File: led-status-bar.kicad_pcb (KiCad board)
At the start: 2 copper layers, 2 parts

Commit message: Revision 1 commit
- Added all required connections to the PCB
- Fabrication revision 1
- Added README with suitable information
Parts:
- added C1: 100nF, Capacitor_SMD:C_0603_1608Metric_Pad1.08x0.95mm_HandSolder, F.Cu at (126.1, 79.8)
- added C2: 100nF, Capacitor_SMD:C_0603_1608Metric_Pad1.08x0.95mm_HandSolder, F.Cu at (126.1, 85.9)
- added C3: 100nF, Capacitor_SMD:C_0603_1608Metric_Pad1.08x0.95mm_HandSolder, F.Cu at (126.1, 92.1)
- added C4: 100nF, Capacitor_SMD:C_0603_1608Metric_Pad1.08x0.95mm_HandSolder, F.Cu at (126.1, 98.2)
- added C5: 100nF, Capacitor_SMD:C_0603_1608Metric_Pad1.08x0.95mm_HandSolder, F.Cu at (126.1, 104.3)
- added D1: WS2812B, LED_SMD:LED_WS2812B_PLCC4_5.0x5.0mm_P3.2mm, F.Cu at (131.1, 79.8)
- added D2: WS2812B, LED_SMD:LED_WS2812B_PLCC4_5.0x5.0mm_P3.2mm, F.Cu at (131.1, 85.9)
- added D3: WS2812B, LED_SMD:LED_WS2812B_PLCC4_5.0x5.0mm_P3.2mm, F.Cu at (131.1, 92.0)
- added D4: WS2812B, LED_SMD:LED_WS2812B_PLCC4_5.0x5.0mm_P3.2mm, F.Cu at (131.1, 98.1)
- added D5: WS2812B, LED_SMD:LED_WS2812B_PLCC4_5.0x5.0mm_P3.2mm, F.Cu at (131.1, 104.2)
- added H1: MountingHole, MountingHole:MountingHole_3.2mm_M3-smallBorder, F.Cu at (131.3, 61.2)
- added H2: MountingHole, MountingHole:MountingHole_3.2mm_M3-smallBorder, F.Cu at (131.3, 111.5)
- added J1: Conn_01x03, Connector_PinHeader_2.54mm:PinHeader_1x03_P2.54mm_Vertical, F.Cu at (128.8, 67.1)
- added Q1: SS8050-G, Package_TO_SOT_SMD:SOT-23, F.Cu at (129.0, 71.9)
- added R1: 1k, Resistor_SMD:R_0603_1608Metric_Pad0.98x0.95mm_HandSolder, F.Cu at (131.8, 71.9)
- moved G*** 150.1 mm to (129.8, 72.4), turned to -90 degrees
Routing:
- net VSS: track 0.00 -> 55.0 mm
- net GND: track 0.00 -> 14.0 mm, vias 0 -> 10
- net Net-(D1-Pad4): track 0.00 -> 7.27 mm
- net Net-(D4-Pad2): track 0.00 -> 6.10 mm
- net Net-(D3-Pad2): track 0.00 -> 6.10 mm
- net Net-(D2-Pad2): track 0.00 -> 6.10 mm
- net Net-(D1-Pad2): track 0.00 -> 6.10 mm
- net LED_CTRL: track 0.00 -> 4.22 mm
- net Net-(Q1-Pad1): track 0.00 -> 3.12 mm
- added copper zone on B.Cu, net GND
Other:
- board outline added: 15 x 57.4 mm
- board text added: "RGB-Led Status Bar v1.0 (2023)"

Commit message: Added pinout to back of board
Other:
- board text added: "DTA"
- board text added: "GND"
- board text added: "VSS"
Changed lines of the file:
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@@
   )
   (gr_rect (start 122.682 57.912) (end 137.668 115.316) (layer "Edge.Cuts") (width 0.2) (fill none))
+  (gr_text "DTA" (at 131.318 64.516) (layer "B.SilkS")
+    (effects (font (size 1 1) (thickness 0.15)) (justify mirror))
+  )
+  (gr_text "GND" (at 134.62 64.516) (layer "B.SilkS")
+    (effects (font (size 1 1) (thickness 0.15)) (justify mirror))
+  )
+  (gr_text "VSS" (at 128.016 64.516) (layer "B.SilkS")
+    (effects (font (size 1 1) (thickness 0.15)) (justify mirror))
+  )
   (gr_text "RGB-Led Status Bar\nv1.0 (2023)" (at 130.556 74.93 90) (layer "B.SilkS")
     (effects (font (size 1 1) (thickness 0.15)) (justify left mirror))

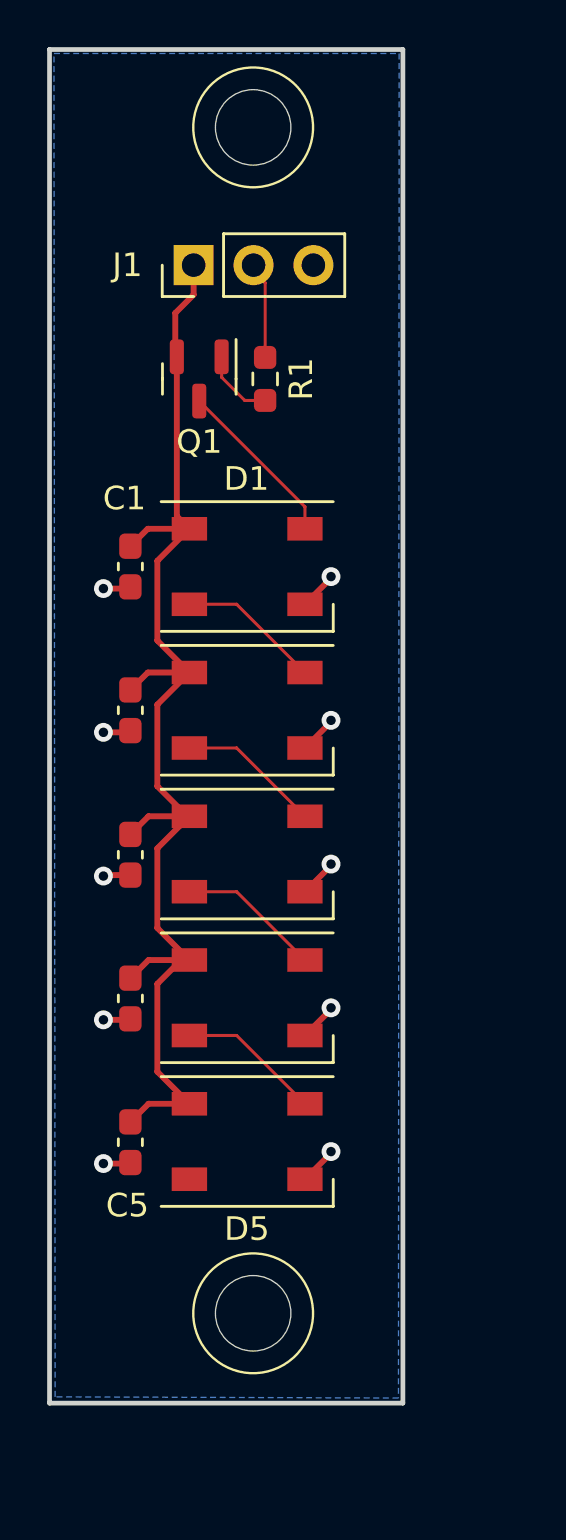
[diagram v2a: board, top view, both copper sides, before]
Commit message: Updated template for KiCAD 7
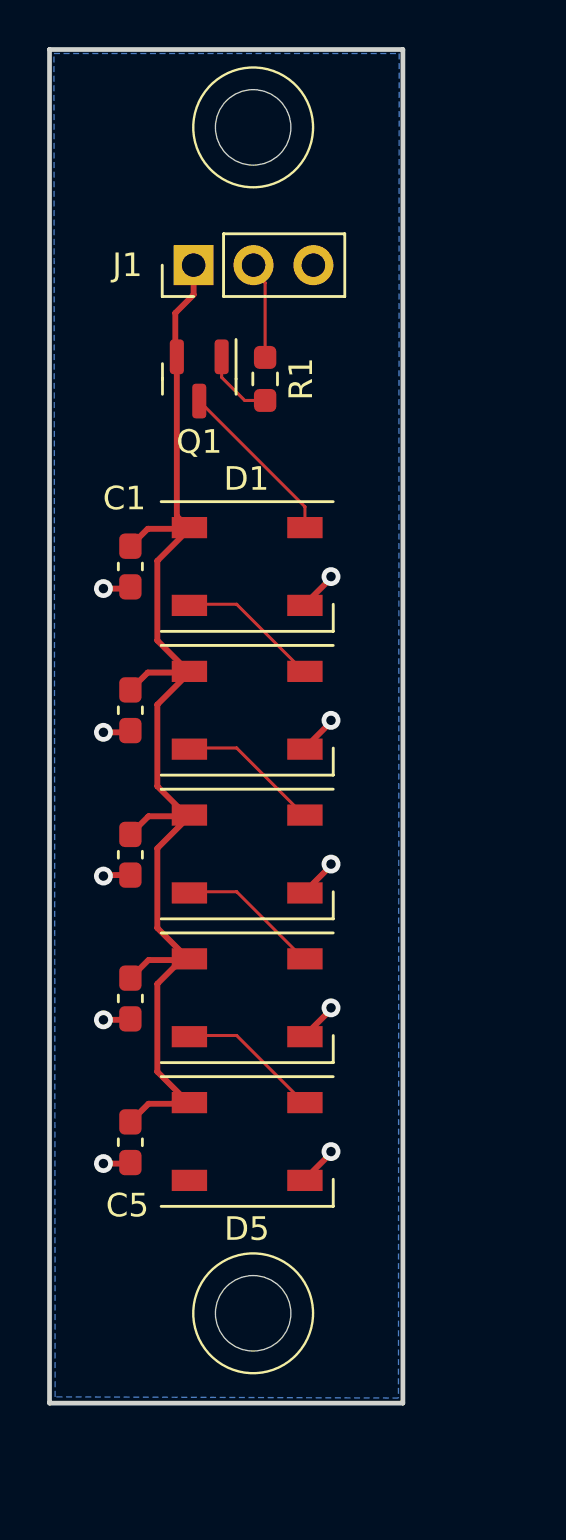
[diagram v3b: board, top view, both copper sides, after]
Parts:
- removed the G*** at (22.4, 182.3)
- G***: footprint LOGO -> Chof747 Logos:LOGO small
- H1, H2: footprint MountingHole:MountingHole_3.2mm_M3-smallBorder -> Chof747 Footprints:MountingHole_3.2mm_M3-smallBorder

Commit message: Revision 1.1 - Correcting error with Level shift
- Changed BJTs with N-Channel Mosfets
- Added resistors accordingly
- Added an outbound connector
- Added Vref (3v3) to allow daisy chaining
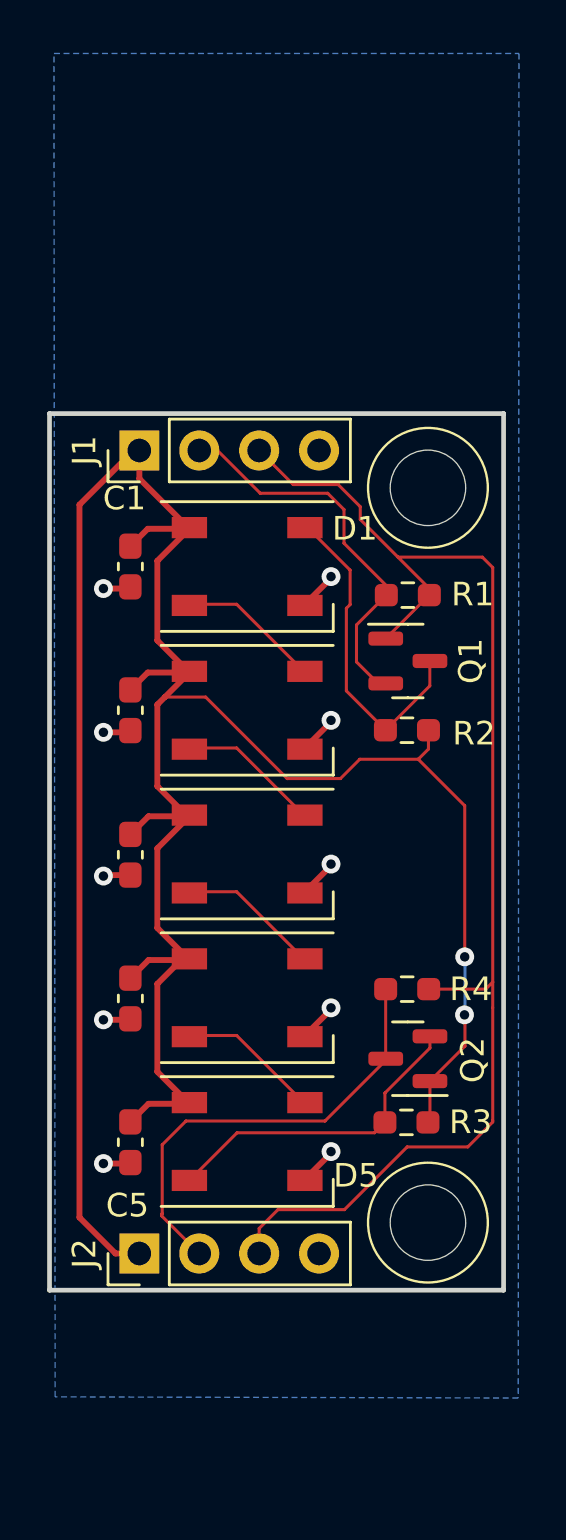
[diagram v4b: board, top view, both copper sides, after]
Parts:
- added J2: Conn_01x03, Connector_PinHeader_2.54mm:PinHeader_1x04_P2.54mm_Vertical, F.Cu at (126.5, 109.0)
- added Q2: 2N7002, Package_TO_SOT_SMD:SOT-23, F.Cu at (137.9, 100.7)
- added R2: 10k, Resistor_SMD:R_0603_1608Metric_Pad0.98x0.95mm_HandSolder, F.Cu at (137.8, 86.8)
- added R3: 10k, Resistor_SMD:R_0603_1608Metric_Pad0.98x0.95mm_HandSolder, F.Cu at (137.8, 103.4)
- added R4: 10k, Resistor_SMD:R_0603_1608Metric_Pad0.98x0.95mm_HandSolder, F.Cu at (137.8, 97.8)
- J1: footprint Connector_PinHeader_2.54mm:PinHeader_1x03_P2.54mm_Vertical -> Connector_PinHeader_2.54mm:PinHeader_1x04_P2.54mm_Vertical
- Q1: value SS8050-G -> 2N7002
- R1: value 1k -> 10k
- moved G*** 23.5 mm to (130.5, 95.9)
- moved H1 17.0 mm to (138.7, 76.5)
- moved Q1 14.9 mm to (137.9, 83.8), turned to 0 degrees
- moved R1 11.0 mm to (137.9, 81.0), turned to 180 degrees
- moved H2 8.35 mm to (138.7, 107.7)
- moved J1 8.19 mm to (126.5, 74.9)
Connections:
- C1 pad 1: VSS -> VDD
- C2 pad 1: VSS -> VDD
- C3 pad 1: VSS -> VDD
- C4 pad 1: VSS -> VDD
- C5 pad 1: VSS -> VDD
- D1 pad 1: VSS -> VDD
- D2 pad 1: VSS -> VDD
- D3 pad 1: VSS -> VDD
- D4 pad 1: VSS -> VDD
- D5 pad 1: VSS -> VDD
- D5 pad 2: unconnected-(D5-Pad2) -> Net-(D5-DOUT)
- J1 pad 1: VSS -> VDD
- J1 pad 2: LED_CTRL -> LED_CTRL_IN
- J1 pad 3: GND -> VREF
- Q1 pad 1: Net-(Q1-Pad1) -> VREF
- Q1 pad 2: VSS -> LED_CTRL_IN
- R1 pad 1: Net-(Q1-Pad1) -> VREF
- R1 pad 2: LED_CTRL -> LED_CTRL_IN
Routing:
- net VDD: track 0.00 -> 115.1 mm, vias 0 -> 2
- net VREF: track 0.00 -> 56.2 mm
- net VSS: track 55.0 -> 0.00 mm
- net LED_CTRL_OUT: track 0.00 -> 19.3 mm
- net LED_CTRL_IN: track 0.00 -> 15.7 mm
- net Net-(D5-DOUT): track 0.00 -> 13.8 mm
- net Net-(D1-DIN): track 7.27 -> 13.9 mm
- net LED_CTRL: track 4.22 -> 0.00 mm
- net Net-(Q1-Pad1): track 3.12 -> 0.00 mm
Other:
- board size 15 x 57.4 mm -> 19.3 x 37.2 mm
- board text added: "VDD"
- board text added: "VREF"
- board text removed: "VSS"

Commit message: Corrected fab descriptions of connectors
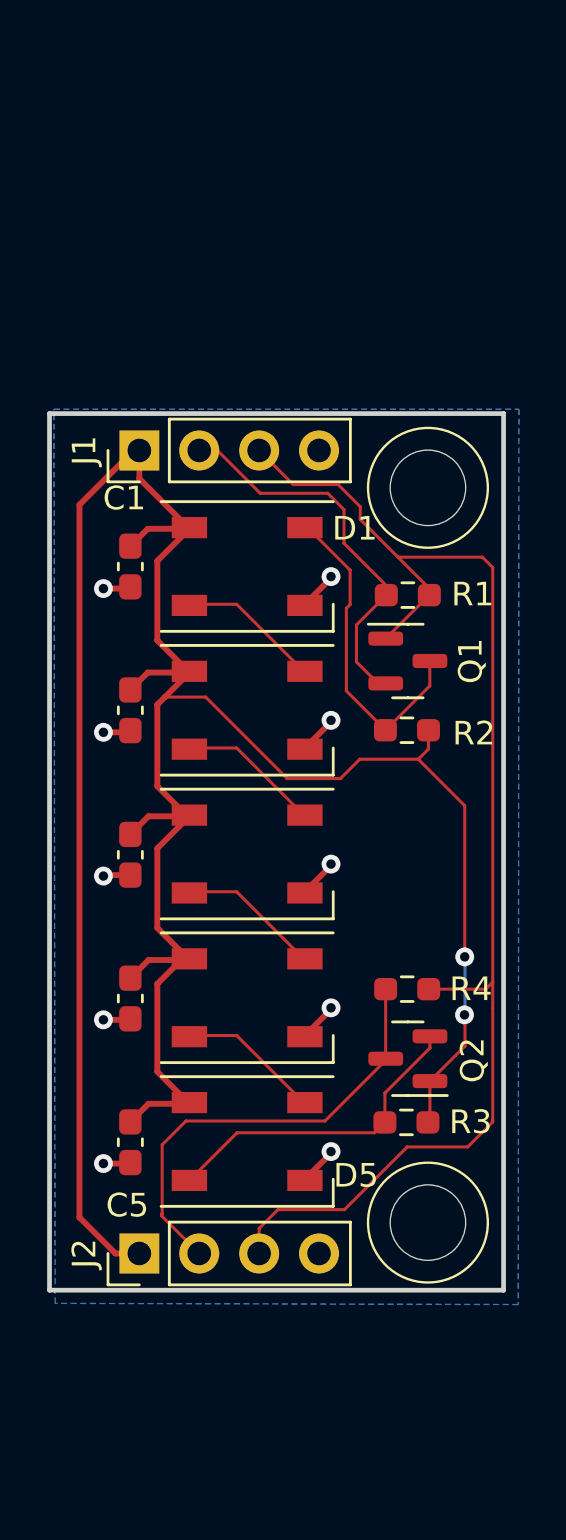
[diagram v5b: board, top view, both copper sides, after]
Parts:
- J1, J2: value Conn_01x03 -> Conn_01x04
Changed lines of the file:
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@@
         (effects (font (size 1 1) (thickness 0.15)))
     )
-    (fp_text value "Conn_01x03" (at -3.01 2.146 180) (layer "F.Fab")
+    (fp_text value "Conn_01x04" (at -2.77 4.028 180) (layer "F.Fab")
         (effects (font (size 1 1) (thickness 0.15)))
     )
@@
         (effects (font (size 1 1) (thickness 0.15)))
     )
-    (fp_text value "Conn_01x03" (at 0 9.95 90) (layer "F.Fab")
+    (fp_text value "Conn_01x04" (at 2.756 4.328 180) (layer "F.Fab")
         (effects (font (size 1 1) (thickness 0.15)))
     )
@@
     (polygon
       (pts
-        (xy 142.56 115.1)
-        (xy 122.92 115.05)
-        (xy 122.87 58.08)
-        (xy 142.59 58.08)
+        (xy 142.56 111.135075)
+        (xy 122.92 111.085075)
+        (xy 122.87 73.165075)
+        (xy 142.59 73.165075)
       )
     )

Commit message: Final version for rev. 1.1
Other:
- board text added: "G"
- board text removed: "GND"
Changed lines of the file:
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@@
   (gr_rect locked (start 122.682 73.352) (end 141.938 110.526)
     (stroke (width 0.2) (type solid)) (fill none) (layer "Edge.Cuts"))
-  (gr_text "DTA" (at 128.778 77.47) (layer "B.SilkS")
+  (gr_text "DTA" (at 128.524 77.216) (layer "B.SilkS")
     (effects (font (size 1 1) (thickness 0.15)) (justify mirror))
   )
-  (gr_text "VREF" (at 132.08 77.47) (layer "B.SilkS")
+  (gr_text "VREF" (at 132.207 77.216) (layer "B.SilkS")
     (effects (font (size 1 1) (thickness 0.15)) (justify mirror))
   )
-  (gr_text "GND" (at 135.382 77.47) (layer "B.SilkS")
+  (gr_text "G" (at 135.001 77.216) (layer "B.SilkS")
     (effects (font (size 1 1) (thickness 0.15)) (justify mirror))
   )
-  (gr_text "VDD" (at 125.222 77.47) (layer "B.SilkS")
+  (gr_text "VDD" (at 125.095 77.216) (layer "B.SilkS")
     (effects (font (size 1 1) (thickness 0.15)) (justify mirror))
   )
@@
   )
   (dimension (type aligned) (layer "Cmts.User")
-    (pts (xy 122.68 115.26) (xy 137.68 115.23))
+    (pts (xy 122.682 110.526) (xy 141.938 110.526))
     (height 5.860348)
-    (gr_text "15.0000 mm" (at 130.189421 119.955338 0.1145914062) (layer "Cmts.User")
+    (gr_text "19.2560 mm" (at 132.31 115.236348) (layer "Cmts.User")
       (effects (font (size 1 1) (thickness 0.15)))
     )
@@
   )
   (dimension (type aligned) (layer "Cmts.User")
-    (pts (xy 122.68 57.88) (xy 122.7 115.25))
+    (pts (xy 126.492 74.916) (xy 126.492 108.97))
     (height 5.108925)
-    (gr_text "57.3700 mm" (at 119.381075 86.566153 270.0199741) (layer "Cmts.User")
+    (gr_text "34.0540 mm" (at 119.583075 91.943 90) (layer "Cmts.User")
       (effects (font (size 1.5 1.5) (thickness 0.3)))
     )

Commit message: Minor change: replaced pin headers with angled ones
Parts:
- J1: footprint Connector_PinHeader_2.54mm:PinHeader_1x04_P2.54mm_Vertical -> Connector_PinHeader_2.54mm:PinHeader_1x04_P2.54mm_Horizontal
- J2: footprint Connector_PinHeader_2.54mm:PinHeader_1x04_P2.54mm_Vertical -> Connector_PinSocket_2.54mm:PinSocket_1x04_P2.54mm_Horizontal
